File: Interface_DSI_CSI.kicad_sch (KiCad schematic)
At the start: 3 parts

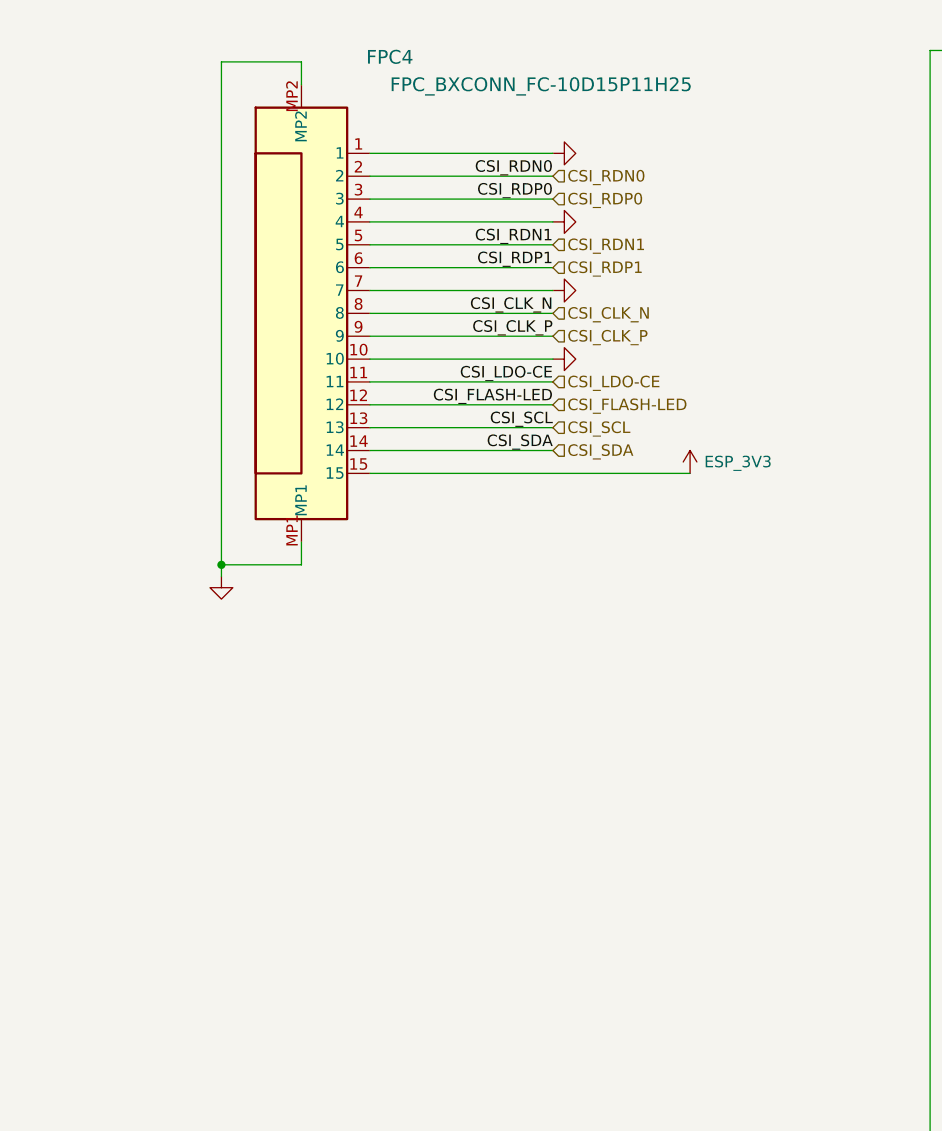
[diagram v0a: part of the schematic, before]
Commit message: QSPI Memory Bus
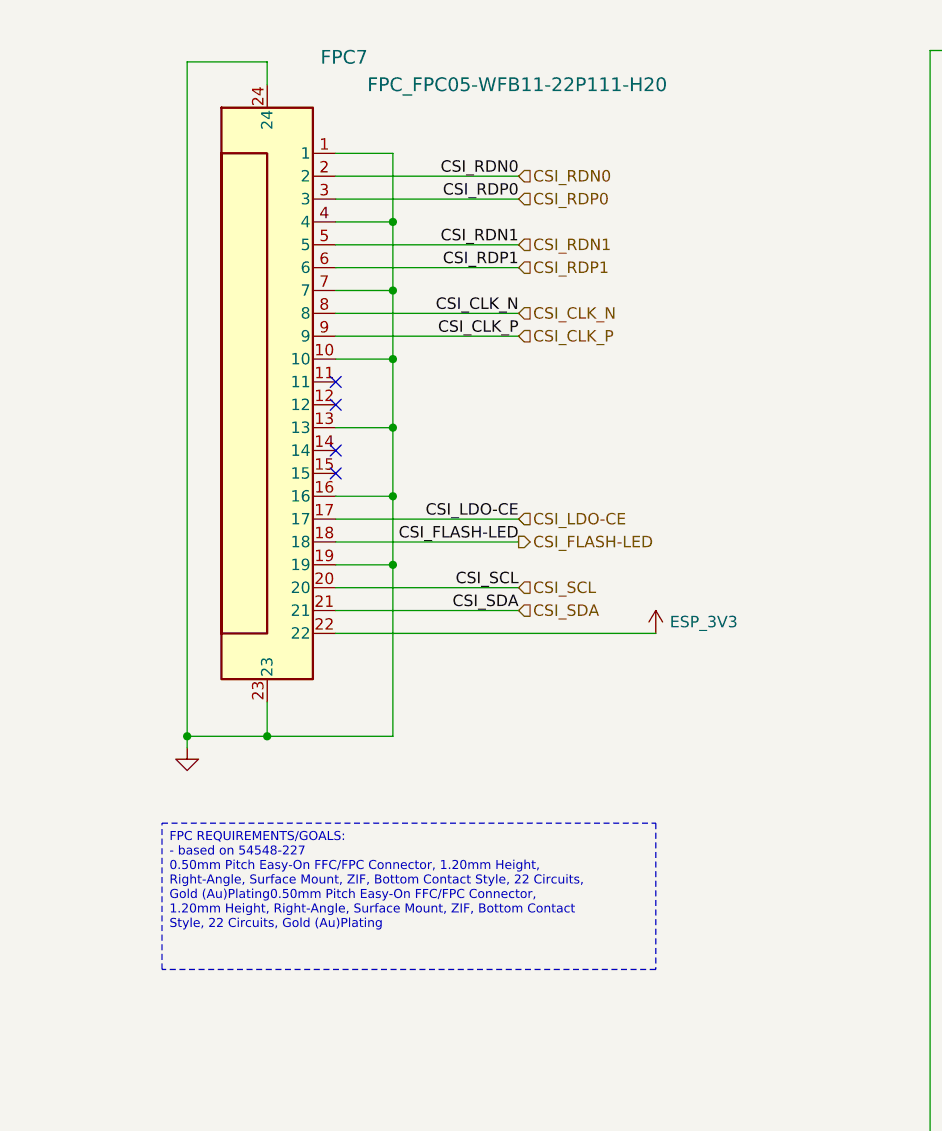
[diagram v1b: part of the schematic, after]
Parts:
- removed FPC4: FPC_BXCONN_FC-10D15P11H25, Personal_Project:FPC_BXCONN_FC-10D15P11H25, symbol Personal_Projects:FPC_BXCONN_FC-10D15P11H25
- added FPC7: FPC_FPC05-WFB11-22P111-H20, Personal_Project:FPC_FPC05-WFB11-22P111-H20, symbol Personal_Projects:FPC_FPC05-WFB11-22P111-H20
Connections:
- net CSI_CLK_N: now also FPC7.8
- net CSI_CLK_P: now also FPC7.9
- net CSI_FLASH-LED: now also FPC7.18
- net CSI_LDO-CE: now also FPC7.17
- net CSI_RDN0: now also FPC7.2
- net CSI_RDN1: now also FPC7.5
- net CSI_RDP0: now also FPC7.3
- net CSI_RDP1: now also FPC7.6
- net CSI_SCL: now also FPC7.20
- net CSI_SDA: now also FPC7.21
- net ESP_3V3: now also FPC7.22
- net GND: now also FPC7.1, FPC7.10, FPC7.13, FPC7.16, FPC7.19, FPC7.23, FPC7.24, FPC7.4, FPC7.7
- no-connect marks 1 -> 5

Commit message: Interface Update
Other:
- company: (none) -> Peter Hancak
- title: (none) -> ESP32P4C5_BOARD
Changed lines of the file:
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@@
 	(generator_version "8.0")
 	(paper "A4")
+	(title_block
+		(title "ESP32P4C5_BOARD")
+		(date "2026-06-01")
+		(rev "A")
+		(company "Peter Hancak")
+	)
 	(junction
 		(at 121.92 115.57)

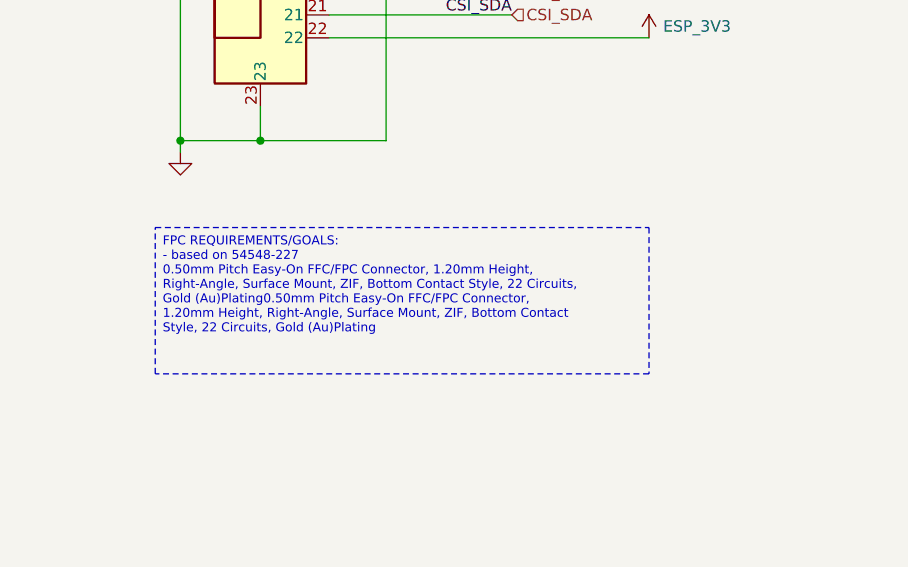
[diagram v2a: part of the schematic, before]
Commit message: Small trace layout fixes
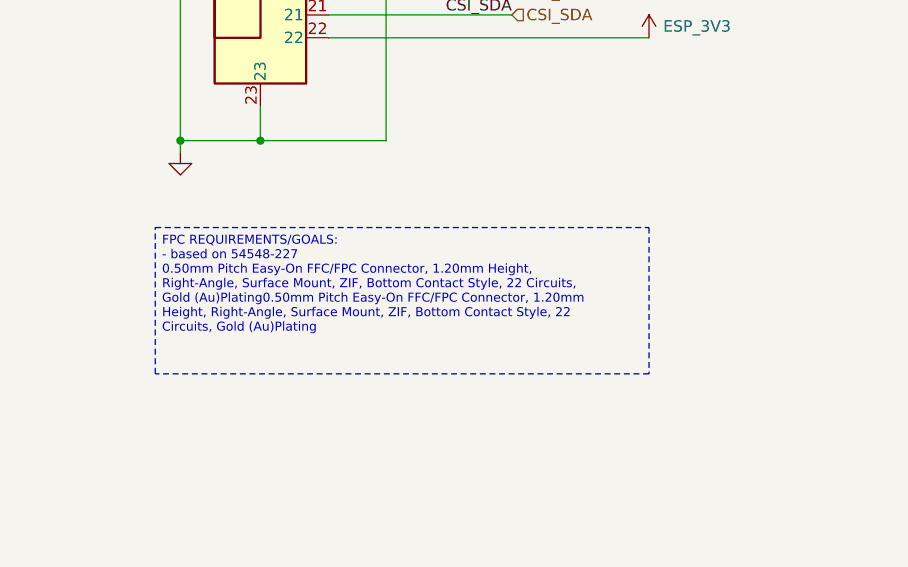
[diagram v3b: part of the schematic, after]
